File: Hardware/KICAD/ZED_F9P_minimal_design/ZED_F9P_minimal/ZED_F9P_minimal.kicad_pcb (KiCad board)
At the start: 2 copper layers, 60 x 43.5 mm, 28 parts, among them U2 LM1086IT-ADJ/NOPB

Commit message: files generation
gerbers an drill generation
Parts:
- added REF: NPTH_test, VIA:NPTH_test, F.Cu at (77.4, 61.4)
- added REF: NPTH_test, VIA:NPTH_test, F.Cu at (22.6, 20.9)
- added REF: NPTH_test, VIA:NPTH_test, F.Cu at (22.6, 61.4)
- added REF: NPTH_test, VIA:NPTH_test, F.Cu at (70.2, 21.0)
- Reg: renamed from U2; moved to F.Cu
- moved C5 1.90 mm to (56.3, 44.9)
- moved SMA 1.23 mm to (77.5, 27.5)
- moved JP3 1.23 mm to (66.0, 33.2)
- moved JP4 1.23 mm to (70.0, 33.2)
- moved C6 1.23 mm to (56.3, 40.2)
- moved JP1 1.23 mm to (67.3, 51.2)
- moved JP2 1.23 mm to (71.3, 51.2)
- moved OPA2365AID 1.23 mm to (68.4, 42.3)
- moved R2 1.23 mm to (59.3, 44.2)
- moved R3 1.23 mm to (62.1, 44.2)
- moved R6 1.23 mm to (59.3, 40.4)
- moved R7 1.23 mm to (62.1, 40.4)
- moved TP1 1.23 mm to (60.8, 24.0), turned to 180 degrees
- moved TP2 1.23 mm to (63.3, 50.2)
- moved TP3 1.23 mm to (56.0, 35.2)
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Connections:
- INPUT pad 19: (no net) -> GND
- INPUT pad 20: (no net) -> GND
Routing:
- net /5V-IN: track 14.6 -> 12.9 mm
- net /3V3-jumper: track 48.6 -> 49.8 mm
- net /5V-jumper: track 76.6 -> 77.9 mm
- net /pt div: track 27.8 -> 28.9 mm
- net /12V: track 45.7 -> 46.5 mm
- net /3v3_puce: track 43.7 -> 43.4 mm, vias 4 -> 2
- net GND: vias 322 -> 324
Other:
- board size 60 x 43.5 mm -> 60 x 45.5 mm

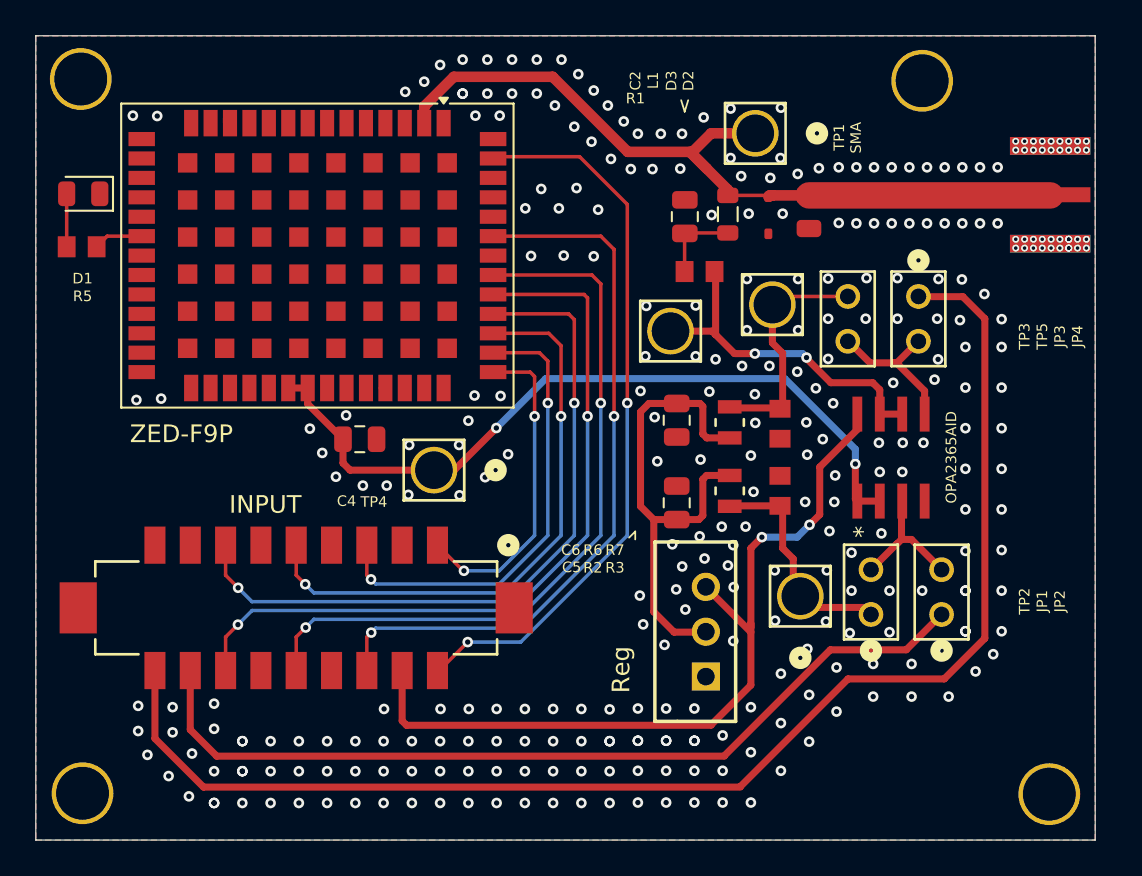
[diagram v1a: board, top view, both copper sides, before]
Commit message: modifications
corrected critical mistakes on rf input
added power on state led
removed RF input testpoint
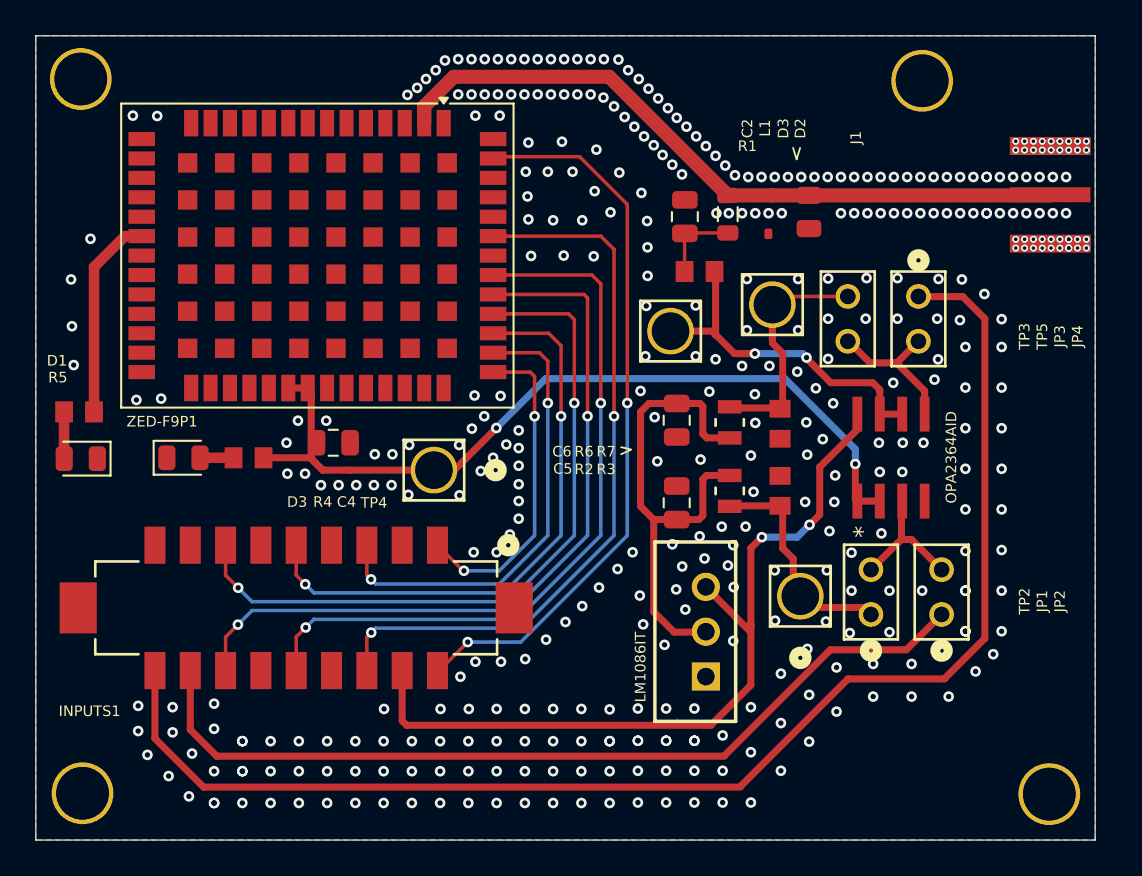
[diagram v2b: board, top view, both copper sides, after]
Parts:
- removed TP1: TestPoint, TestPoint:CONN1_5011_KEY
- added D3: LED_rouge, LED_SMD:LED_0805_2012Metric, F.Cu at (28.4, 42.4)
- added R4: 330, res_SMD_330ohm:RC0805N_YAG, F.Cu at (32.1, 42.4)
- LM1086IT: renamed from Reg; value LM1086IT-ADJ/NOPB -> ~
- moved D1 15.0 mm to (22.6, 42.4)
- moved R5 9.35 mm to (22.5, 39.8)
- moved C4 1.51 mm to (36.9, 41.5)
- renumbered INPUT to INPUTS1, SMA to J1, OPA2365AID to OPA2364AID, ZED-F9P to ZED-F9P1
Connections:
- R5 pad 1: GND -> Net-(ZED-F9P1-RTK_STAT)
- ZED-F9P1 pad 20: GND -> Net-(ZED-F9P1-RTK_STAT)
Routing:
- net Net-(ZED-F9P1-RTK_STAT): track 0.00 -> 11.6 mm
- net /RF_IN: track 46.1 -> 39.9 mm
- net /3v3_puce: track 43.4 -> 48.0 mm
- net GND: track 3.45 -> 0.65 mm, vias 324 -> 409
- net Net-(D3-A): track 0.00 -> 1.90 mm
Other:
- board text added: "PWR ON"
- board text added: "RTK STATUS"
